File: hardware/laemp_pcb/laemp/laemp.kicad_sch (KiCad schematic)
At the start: 23 parts, among them J1 Conn_02x04_Counter_Clockwise, J2 Conn_01x02_Pin, U1 TPS61165DBV, U2 TPS61165DBV, U3 TPS61165DBV, U4 TPS61165DBV, U5 TPS54202DDC

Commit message: added new lib and schematic changes
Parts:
- removed U2, U3, U4: TPS61165DBV, Package_TO_SOT_SMD:SOT-23-6, symbol Driver_LED:TPS61165DBV
- added C10, C11, C12, C7, C8, C9: C, symbol Device:C
- added D10, D11, D12, D14, D15, D16, D18, D19, D20: LED, symbol Device:LED
- added D13, D17, D9: D_Schottky, symbol Device:D_Schottky
- added D5, D6, D7, D8: (no value), symbol laemp:XPLDCL_LED
- added L3, L4, L5: L, symbol Device:L
- added R4, R5, R6: R, symbol Device:R
- added U6, U7, U8: TPS61165DBV, Package_TO_SOT_SMD:SOT-23-6, symbol Driver_LED:TPS61165DBV
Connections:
- net GND: now also C10.2, C11.2, C12.2, C7.2, C8.2, C9.2, R4.2, R5.2, R6.2, U6.4 (GND), U7.4 (GND), U8.4 (GND)
- net VSS: now also C11.1, C7.1, C9.1, L3.1, L4.1, L5.1, U6.1 (VIN), U7.1 (VIN), U8.1 (VIN)
- new net: C10.1, D13.1 (K), D14.2 (A)
- new net: D13.2 (A), L4.2, U7.3 (SW)
- new net: D19.1 (K), D20.2 (A)
- new net: D18.1 (K), D19.2 (A)
- new net: D11.1 (K), D12.2 (A)
- new net: D10.1 (K), D11.2 (A)
- new net: D16.1 (K), R5.1, U7.6 (FB)
- new net: D17.2 (A), L5.2, U8.3 (SW)
- new net: D20.1 (K), R6.1, U8.6 (FB)
- new net: C8.1, D10.2 (A), D9.1 (K)
- new net: D15.1 (K), D16.2 (A)
- new net: D9.2 (A), L3.2, U6.3 (SW)
- new net: C12.1, D17.1 (K), D18.2 (A)
- new net: D14.1 (K), D15.2 (A)
- new net: D12.1 (K), R4.1, U6.6 (FB)
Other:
- note added: "Max Voltage LEDs: Red: 3.2V Green: 3.4V Blue: 3.7V White: 3.6V"

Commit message: added lables to boost converter for the ledso
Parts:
- removed D10, D11, D12: LED, symbol Device:LED
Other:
- note added: "BLUE"
- note added: "GREEN"
- note added: "RED"
- note added: "WHITE"
- moved on the sheet: D5, D6, D7, D8

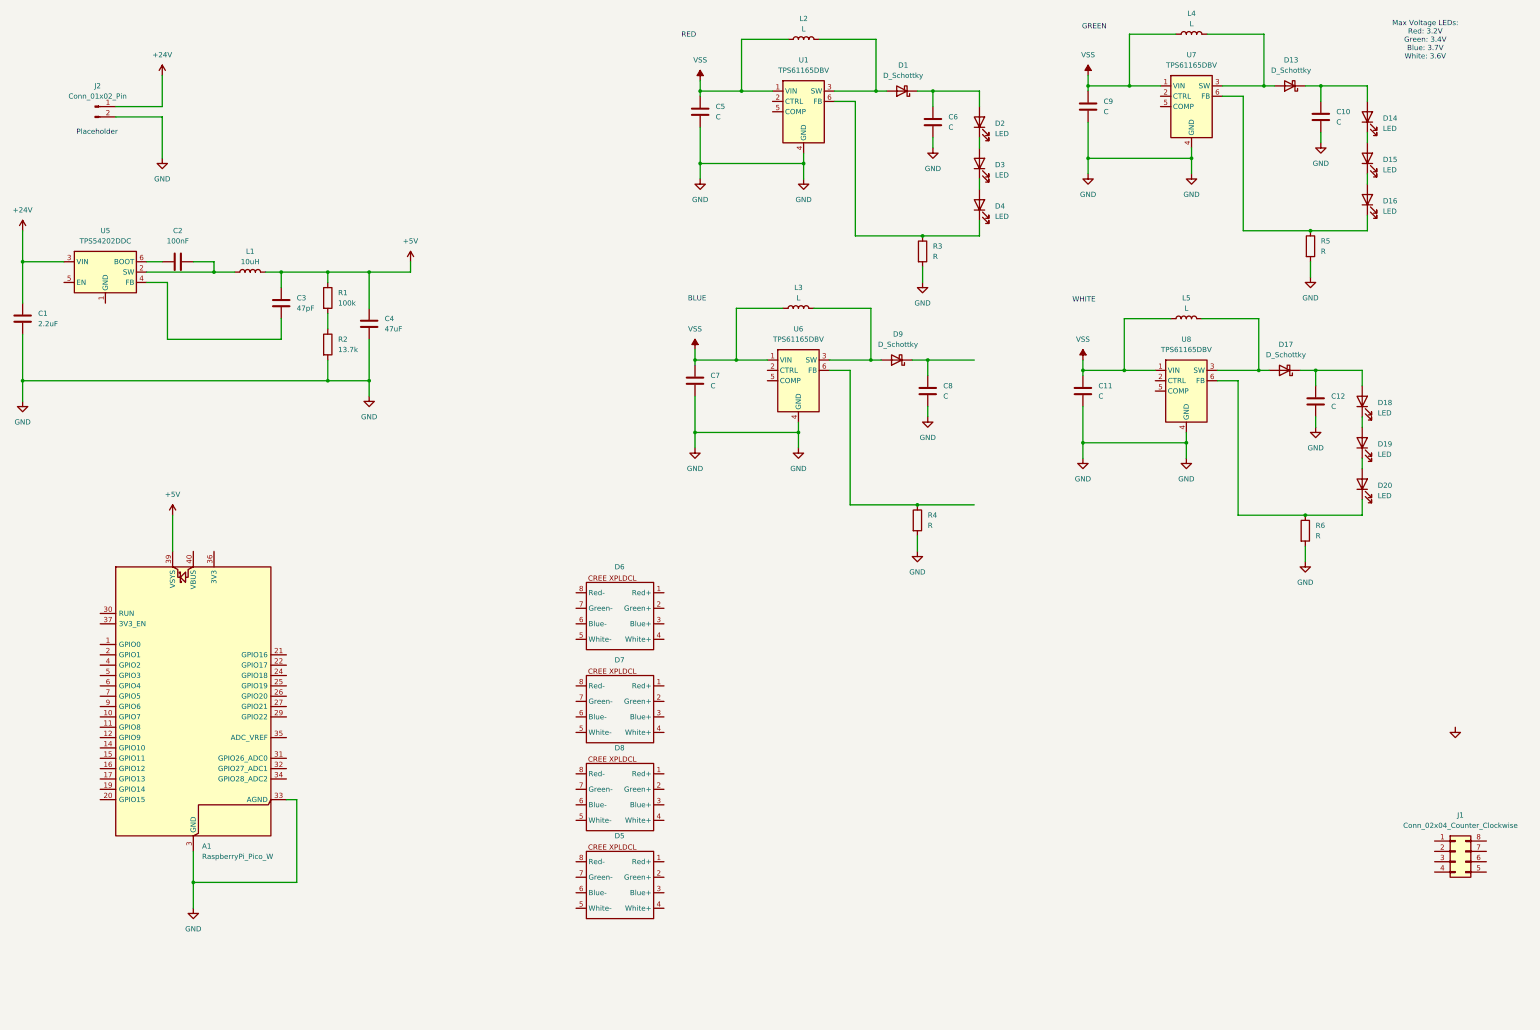
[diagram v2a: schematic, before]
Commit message: added 15V power supply and a total of 8 power LEDs
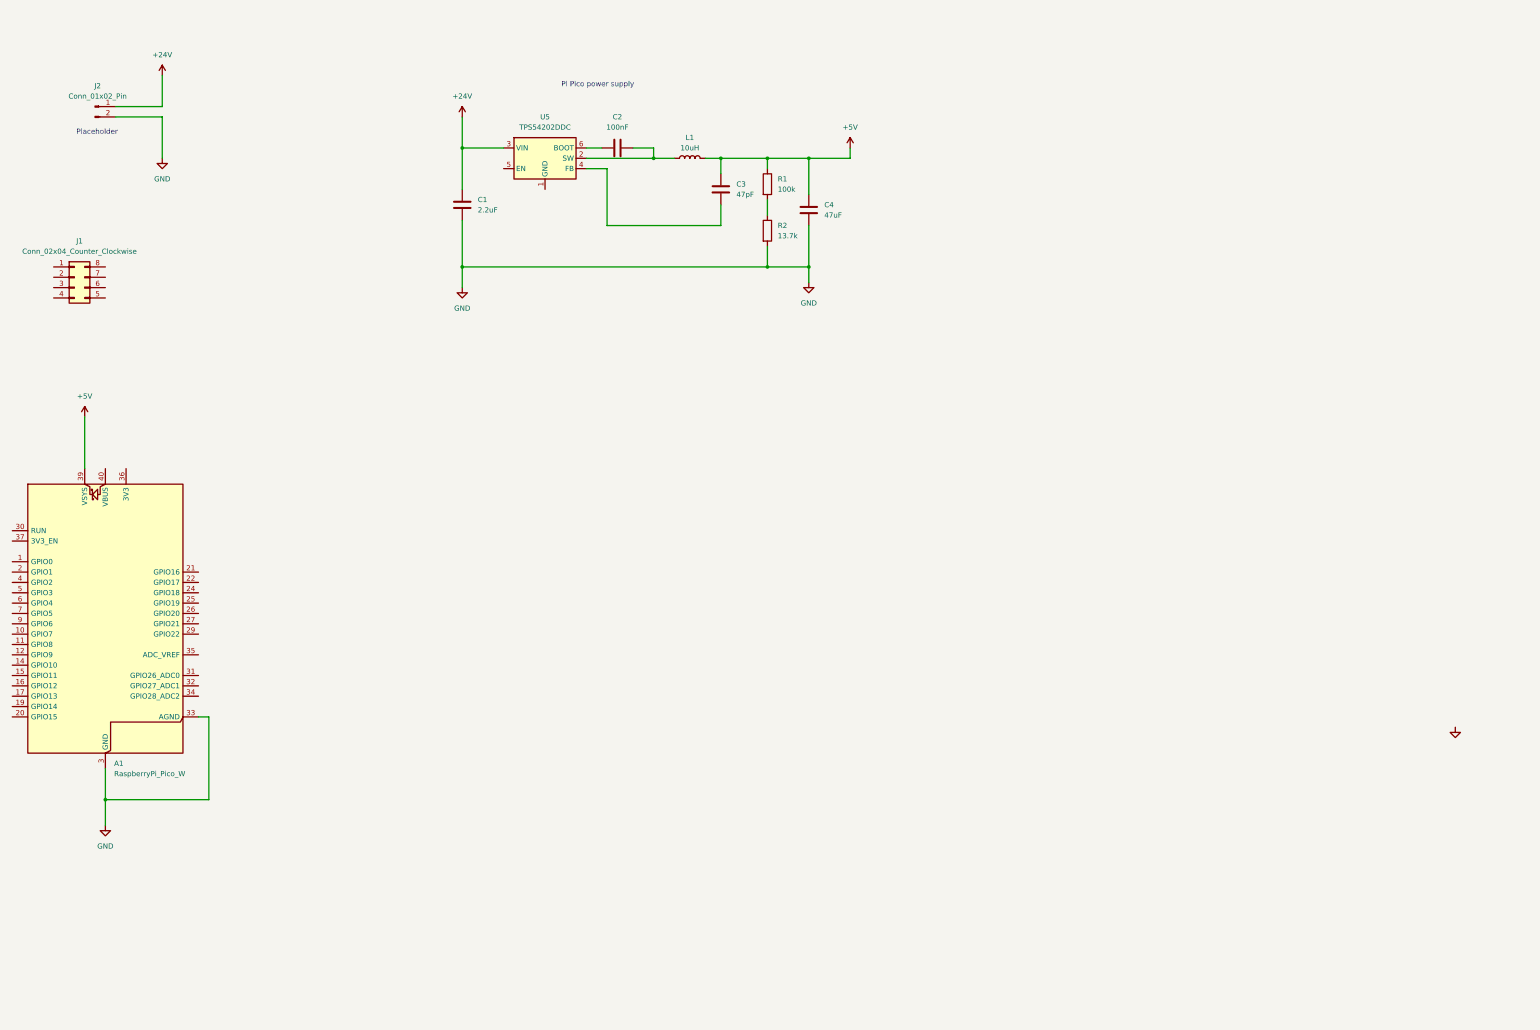
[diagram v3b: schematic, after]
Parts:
- removed C10, C11, C12, C5, C6, C7, C8, C9: C, symbol Device:C
- removed D1, D13, D17, D9: D_Schottky, symbol Device:D_Schottky
- removed D14, D15, D16, D18, D19, D2, D20, D3, D4: LED, symbol Device:LED
- removed D5, D6, D7, D8: (no value), symbol laemp:XPLDCL_LED
- removed L2, L3, L4, L5: L, symbol Device:L
- removed R3, R4, R5, R6: R, symbol Device:R
- removed U1, U6, U7, U8: TPS61165DBV, Package_TO_SOT_SMD:SOT-23-6, symbol Driver_LED:TPS61165DBV
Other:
- note added: "Pi Pico power supply"
- note removed: "BLUE"
- note removed: "GREEN"
- note removed: "Max Voltage LEDs: Red: 3.2V Green: 3.4V Blue: 3.7V White: 3.6V"
- note removed: "RED"
- note removed: "WHITE"
- moved on the sheet: A1, C1, C2, C3, C4, J1, L1, R1, R2, U5

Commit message: updated schematic
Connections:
- net GND: no longer A1.33 (AGND)
- new net AGND: A1.33 (AGND)
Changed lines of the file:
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@@
-	)
-	(junction
-		(at 39.37 212.09)
-		(diameter 0)
-		(color 0 0 0 0)
 	)
 	(junction
@@
 	(wire
 		(pts
-			(xy 64.77 191.77) (xy 64.77 212.09)
-		)
-		(stroke
-			(width 0)
-			(type default)
-		)
-	)
-	(wire
-		(pts
 			(xy 127 52.07) (xy 127 62.23)
 		)
@@
 	(wire
 		(pts
+			(xy 64.77 191.77) (xy 64.77 218.44)
+		)
+		(stroke
+			(width 0)
+			(type default)
+		)
+	)
+	(wire
+		(pts
 			(xy 212.09 81.28) (xy 212.09 85.09)
 		)
@@
 	(wire
 		(pts
-			(xy 64.77 212.09) (xy 39.37 212.09)
-		)
-		(stroke
-			(width 0)
-			(type default)
-		)
-	)
-	(wire
-		(pts
-			(xy 39.37 212.09) (xy 39.37 218.44)
-		)
-		(stroke
-			(width 0)
-			(type default)
-		)
-	)
-	(wire
-		(pts
-			(xy 39.37 204.47) (xy 39.37 212.09)
+			(xy 39.37 204.47) (xy 39.37 218.44)
 		)
 		(stroke
@@
 					(unit 1)
 				)
+			)
+		)
+	)
+	(symbol
+		(lib_id "power:GND")
+		(at 64.77 218.44 0)
+		(unit 1)
+		(body_style 1)
+		(exclude_from_sim no)
+		(in_bom yes)
+		(on_board yes)
+		(in_pos_files yes)
+		(dnp no)
+		(fields_autoplaced yes)
+		(property "Reference" "#PWR035"
+			(at 64.77 224.79 0)
+			(hide yes)
+			(show_name no)
+			(do_not_autoplace no)
+			(effects
+				(font
+					(size 1.27 1.27)
+				)
+			)
+		)
+		(property "Value" "AGND"
+			(at 64.77 223.52 0)
+			(show_name no)
+			(do_not_autoplace no)
+			(effects
+				(font
+					(size 1.27 1.27)
+				)
+			)
+		)
+		(property "Footprint" ""
+			(at 64.77 218.44 0)
+			(hide yes)
+			(show_name no)
+			(do_not_autoplace no)
+			(effects
+				(font
+					(size 1.27 1.27)
+				)
+			)
+		)
+		(property "Datasheet" ""
+			(at 64.77 218.44 0)
+			(hide yes)
+			(show_name no)
+			(do_not_autoplace no)
+			(effects
+				(font
+					(size 1.27 1.27)
+				)
+			)
+		)
+		(property "Description" "Power symbol creates a global label with name \"GND\" , ground"
+			(at 64.77 218.44 0)
+			(hide yes)
+			(show_name no)
+			(do_not_autoplace no)
+			(effects
+				(font
+					(size 1.27 1.27)
+				)
+			)
+		)
+		(pin "1"
+		)
+		(instances
+			(project "laemp"
+				(path "/990afbf2-17b3-4e1d-b2b2-21e40305ab5f"
+					(reference "#PWR035")
+					(unit 1)
+				)
